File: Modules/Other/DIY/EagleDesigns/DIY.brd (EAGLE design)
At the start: 100 x 80 mm, 6 parts

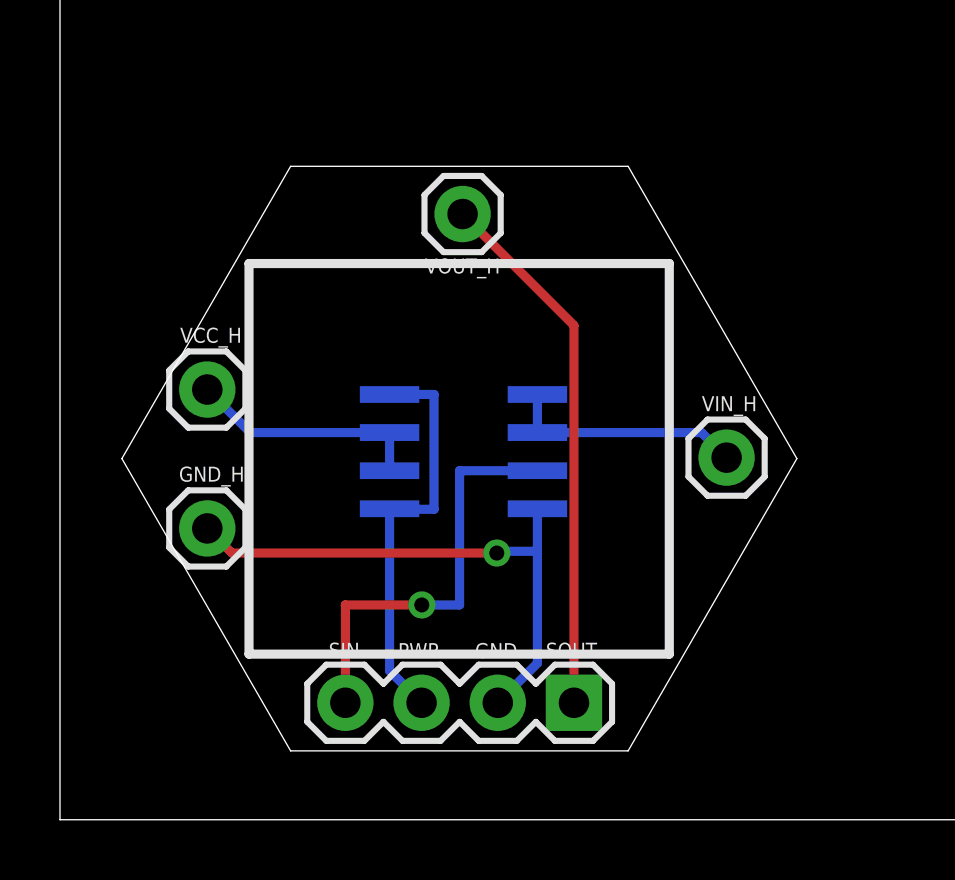
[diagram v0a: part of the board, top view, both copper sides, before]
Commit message: DIY: fixed dimensions #33
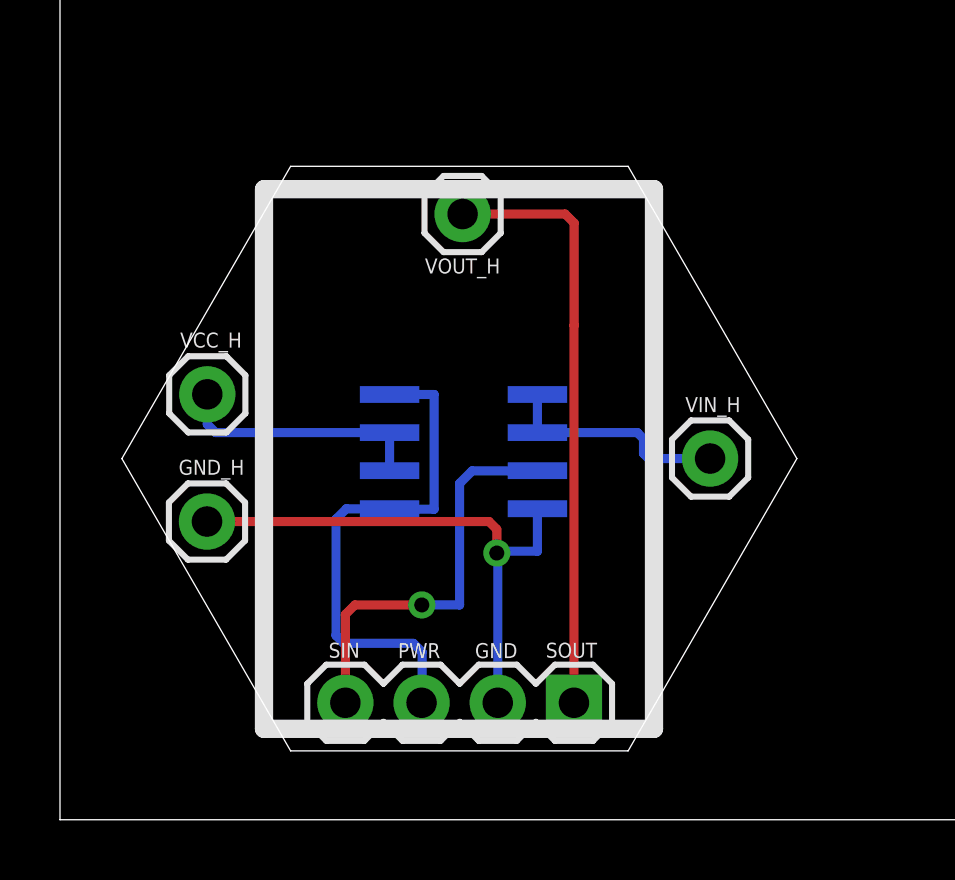
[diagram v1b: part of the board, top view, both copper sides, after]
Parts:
- moved VIN_H 0.55 mm to (21.7, 12.0)
- moved GND_H 0.23 mm to (4.90, 9.94)
- moved VCC_H 0.16 mm to (4.91, 14.2)
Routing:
- net VCC: track 13.7 -> 17.4 mm
- net SOUT: track 17.8 -> 19.8 mm
- net VCC_H: track 7.94 -> 8.46 mm
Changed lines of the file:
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@@
 <?xml version="1.0" encoding="utf-8"?>
 <!DOCTYPE eagle SYSTEM "eagle.dtd">
-<eagle version="7.6.0">
+<eagle version="7.3.0">
 <drawing>
 <settings>
@@
 <layer number="23" name="tOrigins" color="15" fill="1" visible="yes" active="yes"/>
 <layer number="24" name="bOrigins" color="15" fill="1" visible="yes" active="yes"/>
-<layer number="25" name="tNames" color="7" fill="1" visible="yes" active="yes"/>
-<layer number="26" name="bNames" color="7" fill="1" visible="yes" active="yes"/>
-<layer number="27" name="tValues" color="7" fill="1" visible="yes" active="yes"/>
-<layer number="28" name="bValues" color="7" fill="1" visible="yes" active="yes"/>
+<layer number="25" name="tNames" color="7" fill="1" visible="no" active="yes"/>
+<layer number="26" name="bNames" color="7" fill="1" visible="no" active="yes"/>
+<layer number="27" name="tValues" color="7" fill="1" visible="no" active="yes"/>
+<layer number="28" name="bValues" color="7" fill="1" visible="no" active="yes"/>
 <layer number="29" name="tStop" color="7" fill="3" visible="no" active="yes"/>
 <layer number="30" name="bStop" color="7" fill="6" visible="no" active="yes"/>
@@
 <text x="13.8323" y="5.388" size="0.5" layer="21">GND</text>
 <text x="16.1945" y="5.4007" size="0.5" layer="21">SOUT</text>
-<wire x1="6.3" y1="18.54" x2="20.31" y2="18.54" width="0.3048" layer="21"/>
-<wire x1="20.31" y1="18.54" x2="20.31" y2="5.52" width="0.3048" layer="21"/>
-<wire x1="20.31" y1="5.52" x2="6.3" y2="5.52" width="0.3048" layer="21"/>
-<wire x1="6.3" y1="5.52" x2="6.3" y2="18.54" width="0.3048" layer="21"/>
+<wire x1="6.81" y1="21.02" x2="19.8" y2="21.02" width="0.6096" layer="21"/>
+<wire x1="19.8" y1="21.02" x2="19.8" y2="3.03" width="0.6096" layer="21"/>
+<wire x1="19.8" y1="3.03" x2="6.8" y2="3.03" width="0.6096" layer="21"/>
+<wire x1="6.8" y1="3.03" x2="6.8" y2="21.02" width="0.6096" layer="21"/>
 </plain>
 <attributes>
@@
 <attribute name="VALUE" x="12.15" y="17.015" size="1.27" layer="27"/>
 </element>
-<element name="VIN_H" library="SparkFun-Connectors" package="1X01" value="" x="22.22" y="12.07" smashed="yes">
-<attribute name="NAME" x="21.3938" y="13.6188" size="0.5" layer="25"/>
-<attribute name="VALUE" x="20.95" y="8.895" size="1.27" layer="27"/>
+<element name="VIN_H" library="SparkFun-Connectors" package="1X01" value="" x="21.67" y="12.04" smashed="yes">
+<attribute name="NAME" x="20.8438" y="13.5888" size="0.5" layer="25"/>
+<attribute name="VALUE" x="20.4" y="8.865" size="1.27" layer="27"/>
 </element>
-<element name="VCC_H" library="SparkFun-Connectors" package="1X01" value="" x="4.91" y="14.34" smashed="yes">
-<attribute name="NAME" x="4.0038" y="15.8988" size="0.5" layer="25"/>
-<attribute name="VALUE" x="3.64" y="11.165" size="1.27" layer="27"/>
+<element name="VCC_H" library="SparkFun-Connectors" package="1X01" value="" x="4.91" y="14.18" smashed="yes">
+<attribute name="NAME" x="4.0038" y="15.7388" size="0.5" layer="25"/>
+<attribute name="VALUE" x="3.64" y="11.005" size="1.27" layer="27"/>
 </element>
-<element name="GND_H" library="SparkFun-Connectors" package="1X01" value="" x="4.91" y="9.71" smashed="yes">
-<attribute name="NAME" x="3.9638" y="11.2688" size="0.5" layer="25"/>
-<attribute name="VALUE" x="3.64" y="6.535" size="1.27" layer="27"/>
+<element name="GND_H" library="SparkFun-Connectors" package="1X01" value="" x="4.9" y="9.94" smashed="yes">
+<attribute name="NAME" x="3.9538" y="11.4988" size="0.5" layer="25"/>
+<attribute name="VALUE" x="3.63" y="6.765" size="1.27" layer="27"/>
 </element>
 </elements>
@@
 <wire x1="12.47" y1="10.35" x2="10.9862" y2="10.35" width="0.3048" layer="16"/>
 <wire x1="10.9862" y1="10.35" x2="10.9862" y2="10.365" width="0.3048" layer="16"/>
-<wire x1="10.9862" y1="10.365" x2="10.9862" y2="4.965" width="0.3048" layer="16"/>
-<wire x1="10.9862" y1="4.965" x2="12.0523" y2="3.8989" width="0.3048" layer="16"/>
+<wire x1="10.9862" y1="10.365" x2="9.545" y2="10.365" width="0.3048" layer="16"/>
+<wire x1="9.545" y1="10.365" x2="9.2" y2="10.02" width="0.3048" layer="16"/>
+<wire x1="9.2" y1="10.02" x2="9.2" y2="6.14" width="0.3048" layer="16"/>
+<wire x1="9.2" y1="6.14" x2="9.46" y2="5.88" width="0.3048" layer="16"/>
+<wire x1="9.46" y1="5.88" x2="11.78" y2="5.88" width="0.3048" layer="16"/>
+<wire x1="11.78" y1="5.88" x2="12.07" y2="5.59" width="0.3048" layer="16"/>
+<wire x1="12.07" y1="5.59" x2="12.07" y2="3.9166" width="0.3048" layer="16"/>
+<wire x1="12.07" y1="3.9166" x2="12.0523" y2="3.8989" width="0.3048" layer="16"/>
 </signal>
 <signal name="GND">
@@
 <contactref element="OP_AMP" pad="4"/>
 <contactref element="GND_H" pad="1"/>
-<wire x1="14.5923" y1="3.8989" x2="15.9138" y2="5.2204" width="0.3048" layer="16"/>
-<wire x1="15.9138" y1="5.2204" x2="15.9138" y2="8.95" width="0.3048" layer="16"/>
 <wire x1="15.9138" y1="8.95" x2="15.9138" y2="10.365" width="0.3048" layer="16"/>
-<wire x1="4.91" y1="9.71" x2="5.73" y2="8.89" width="0.3048" layer="1"/>
-<wire x1="5.73" y1="8.89" x2="14.56" y2="8.89" width="0.3048" layer="1"/>
 <via x="14.56" y="8.89" extent="1-16" drill="0.5"/>
 <wire x1="14.56" y1="8.89" x2="14.59" y2="8.89" width="0.3048" layer="16"/>
 <wire x1="14.59" y1="8.89" x2="14.65" y2="8.95" width="0.3048" layer="16"/>
 <wire x1="14.65" y1="8.95" x2="15.9138" y2="8.95" width="0.3048" layer="16"/>
+<wire x1="14.5923" y1="3.8989" x2="14.5923" y2="8.8577" width="0.3048" layer="16"/>
+<wire x1="14.5923" y1="8.8577" x2="14.56" y2="8.89" width="0.3048" layer="16"/>
+<wire x1="4.9" y1="9.94" x2="14.3" y2="9.94" width="0.3048" layer="1"/>
+<wire x1="14.3" y1="9.94" x2="14.56" y2="9.68" width="0.3048" layer="1"/>
+<wire x1="14.56" y1="9.68" x2="14.56" y2="8.89" width="0.3048" layer="1"/>
 </signal>
 <signal name="SIN">
 <contactref element="JP1" pad="4"/>
 <contactref element="OP_AMP" pad="3"/>
-<wire x1="9.5123" y1="3.8989" x2="9.5123" y2="7.16" width="0.3048" layer="1"/>
-<wire x1="9.5123" y1="7.16" x2="12.06" y2="7.16" width="0.3048" layer="1"/>
 <via x="12.06" y="7.16" extent="1-16" drill="0.5"/>
 <wire x1="12.06" y1="7.16" x2="13.32" y2="7.16" width="0.3048" layer="16"/>
-<wire x1="13.32" y1="7.16" x2="13.32" y2="11.635" width="0.3048" layer="16"/>
-<wire x1="13.32" y1="11.635" x2="15.9138" y2="11.635" width="0.3048" layer="16"/>
+<wire x1="9.5123" y1="3.8989" x2="9.5123" y2="6.8423" width="0.3048" layer="1"/>
+<wire x1="9.5123" y1="6.8423" x2="9.83" y2="7.16" width="0.3048" layer="1"/>
+<wire x1="9.83" y1="7.16" x2="12.06" y2="7.16" width="0.3048" layer="1"/>
+<wire x1="13.32" y1="7.16" x2="13.32" y2="11.21" width="0.3048" layer="16"/>
+<wire x1="13.32" y1="11.21" x2="13.74" y2="11.63" width="0.3048" layer="16"/>
+<wire x1="13.74" y1="11.63" x2="15.9088" y2="11.63" width="0.3048" layer="16"/>
+<wire x1="15.9088" y1="11.63" x2="15.9138" y2="11.635" width="0.3048" layer="16"/>
 </signal>
 <signal name="VIN">
@@
 <contactref element="VIN_H" pad="1"/>
 <wire x1="15.9138" y1="14.175" x2="15.9138" y2="12.905" width="0.3048" layer="16"/>
-<wire x1="15.9138" y1="12.905" x2="21.385" y2="12.905" width="0.3048" layer="16"/>
-<wire x1="21.385" y1="12.905" x2="22.22" y2="12.07" width="0.3048" layer="16"/>
+<wire x1="15.9138" y1="12.905" x2="19.245" y2="12.905" width="0.3048" layer="16"/>
+<wire x1="19.245" y1="12.905" x2="19.45" y2="12.7" width="0.3048" layer="16"/>
+<wire x1="19.45" y1="12.7" x2="19.45" y2="12.21" width="0.3048" layer="16"/>
+<wire x1="19.45" y1="12.21" x2="19.62" y2="12.04" width="0.3048" layer="16"/>
+<wire x1="19.62" y1="12.04" x2="21.67" y2="12.04" width="0.3048" layer="16"/>
 </signal>
 <signal name="VCC_H">
@@
 <contactref element="VCC_H" pad="1"/>
 <wire x1="10.9862" y1="12.905" x2="10.9862" y2="11.635" width="0.3048" layer="16"/>
-<wire x1="10.9862" y1="12.905" x2="6.345" y2="12.905" width="0.3048" layer="16"/>
-<wire x1="6.345" y1="12.905" x2="4.91" y2="14.34" width="0.3048" layer="16"/>
+<wire x1="10.9862" y1="12.905" x2="5.185" y2="12.905" width="0.3048" layer="16"/>
+<wire x1="5.185" y1="12.905" x2="4.91" y2="13.18" width="0.3048" layer="16"/>
+<wire x1="4.91" y1="13.18" x2="4.91" y2="14.18" width="0.3048" layer="16"/>
 </signal>
 <signal name="SOUT">
@@
 <contactref element="VOUT_H" pad="1"/>
 <wire x1="17.1323" y1="3.8989" x2="17.1323" y2="16.4777" width="0.3048" layer="1"/>
-<wire x1="17.1323" y1="16.4777" x2="13.42" y2="20.19" width="0.3048" layer="1"/>
+<wire x1="13.42" y1="20.19" x2="16.84" y2="20.19" width="0.3048" layer="1"/>
+<wire x1="16.84" y1="20.19" x2="17.14" y2="19.89" width="0.3048" layer="1"/>
+<wire x1="17.14" y1="19.89" x2="17.14" y2="16.4854" width="0.3048" layer="1"/>
+<wire x1="17.14" y1="16.4854" x2="17.1323" y2="16.4777" width="0.3048" layer="1"/>
 </signal>
 </signals>
